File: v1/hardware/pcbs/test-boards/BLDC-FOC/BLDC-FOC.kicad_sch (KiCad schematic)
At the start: 43 parts, among them CN1 HB9500-3, J1 Conn_01x12, J2 Conn_01x10, J3 Conn_02x02_Odd_Even, U7 TXS0108EPW, U8 TCAN1057AVDRQ1

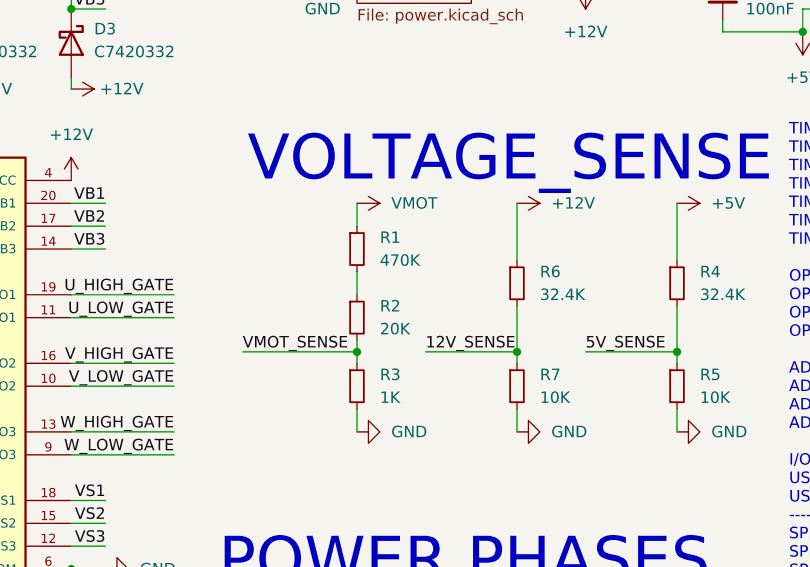
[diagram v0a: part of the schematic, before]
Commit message: corrected VMOT reading voltage divider
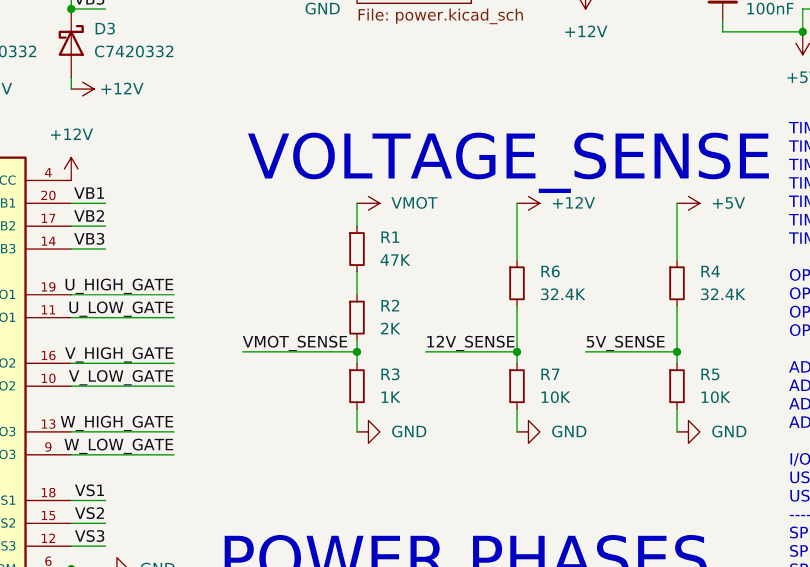
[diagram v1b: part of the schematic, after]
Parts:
- R1: value 470K -> 47K
- R2: value 20K -> 2K
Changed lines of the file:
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@@
 			)
 		)
-		(property "Value" "20K"
+		(property "Value" "2K"
 			(at 138.43 102.87 0)
 			(effects
@@
 		(fields_autoplaced yes)
 		(property "Reference" "R1"
-			(at 138.43 92.7099 0)
+			(at 138.43 92.71 0)
 			(effects
 				(font
@@
 			)
 		)
-		(property "Value" "470K"
+		(property "Value" "47K"
 			(at 138.43 95.25 0)
 			(effects

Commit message: new FOC driver schematic
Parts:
- C1, C2, C3, C4: symbol Device:C_Polarized -> symbols:C_Polarized
- C10, C11, C39, C40, C41, C9: symbol Device:C_Small -> symbols:C_Small
- CN1: symbol EasyEDA:HB9500-3 -> symbols:HB9500-3
- D1, D2, D3: symbol Device:D_Schottky -> symbols:D_Schottky
- GDRV1: symbol SnapEDA:FD6288Q -> symbols:FD6288Q
- J1: symbol Connector_Generic:Conn_01x12 -> symbols:Conn_01x12
- J2: symbol Connector_Generic:Conn_01x10 -> symbols:Conn_01x10
- J3: symbol Connector_Generic:Conn_02x02_Odd_Even -> symbols:Conn_02x02_Odd_Even
- JP1: symbol Jumper:Jumper_3_Bridged12 -> symbols:Jumper_3_Bridged12
- R1, R2, R3, R35, R36, R37, R38, R39, R4, R40, R5, R6, R7: symbol Device:R_Small -> symbols:R_Small
- TP1, TP17, TP2, TP3, TP4, TP5, TP6, TP7: symbol Connector:TestPoint -> symbols:TestPoint
- U1: symbol Custom:STM32G491CET6_breakout -> symbols:STM32G491CET6_breakout
- U7: symbol Logic_LevelTranslator:TXS0108EPW -> symbols:TXS0108EPW
- U8: symbol EasyEDA:TCAN1057AVDRQ1 -> symbols:TCAN1057AVDRQ1
